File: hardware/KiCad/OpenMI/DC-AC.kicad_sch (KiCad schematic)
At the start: 30 parts, among them Q2 IPL60R125P7, Q3 IPL60R125P7, U1 IRS2304S

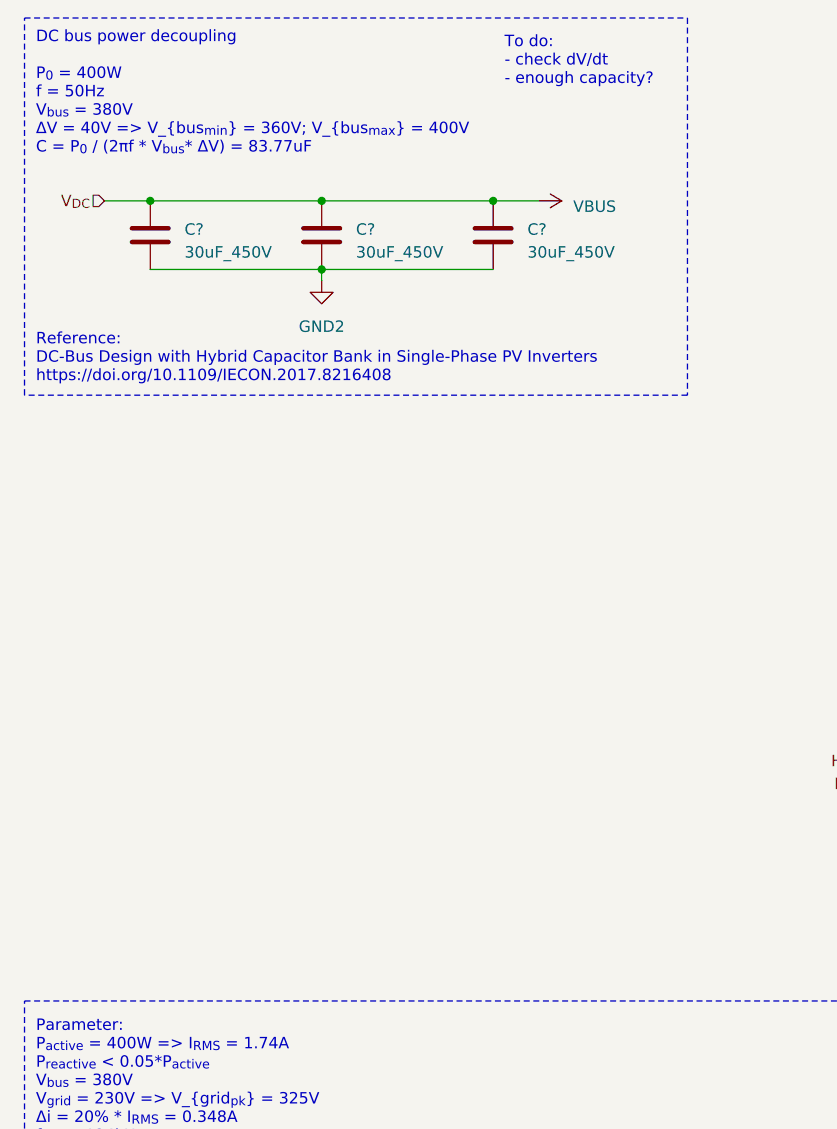
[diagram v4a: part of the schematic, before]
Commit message: feat(hw): Add DC bus voltage sensing
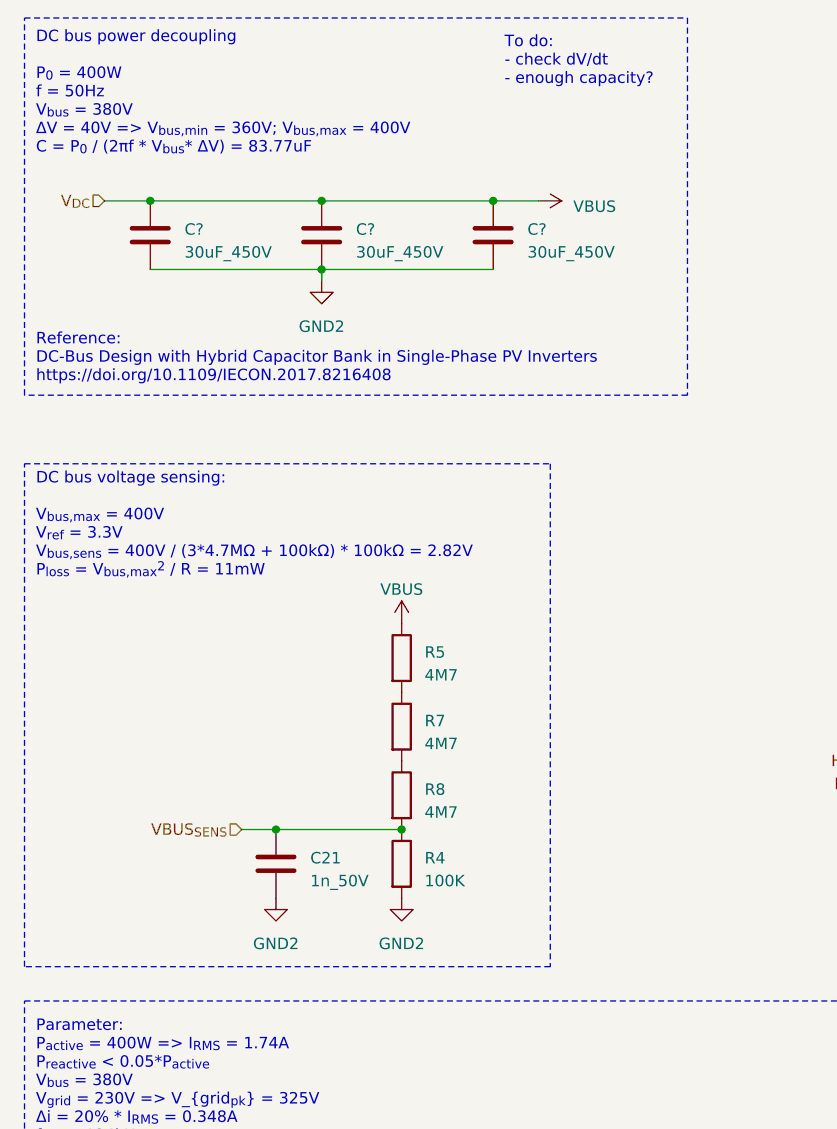
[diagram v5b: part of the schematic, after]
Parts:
- added C21: 1n_50V, Capacitor_SMD:C_0603_1608Metric, symbol _C_0603:1n_50V
- added R4: 100K, Resistor_SMD:R_0603_1608Metric, symbol _R_0603:100K
- added R5, R7, R8: 4M7, Resistor_SMD:R_1206_3216Metric, symbol _R_1206:4M7
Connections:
- net GND: now also C21.2, R4.2
- net VBUS: now also R5.1
- new net: R5.2, R7.1
- new net: R7.2, R8.1
- new net VBUS_{SENS}: C21.1, R4.1, R8.2
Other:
- note added: "DC bus power decoupling P_{0} = 400W f = 50Hz V_{bus} = 380V ΔV = 40V => V_{bus,min} = 360V; V_{bus,max} = 400V C = P_{0} / (2πf * V_{bus}* ΔV) = 83.77uF"
- note added: "DC bus voltage sensing: V_{bus,max} = 400V V_{ref} = 3.3V V_{bus,sens} = 400V / (3*4.7MΩ + 100kΩ) * 100kΩ = 2.82V P_{loss} = V_{bus,max}^{2} / R = 11mW"
- note removed: "DC bus power decoupling P_{0} = 400W f = 50Hz V_{bus} = 380V ΔV = 40V => V_{bus_{min}} = 360V; V_{bus_{max}} = 400V C = P_{0} / (2πf * V_{bus}* ΔV) = 83.77uF"

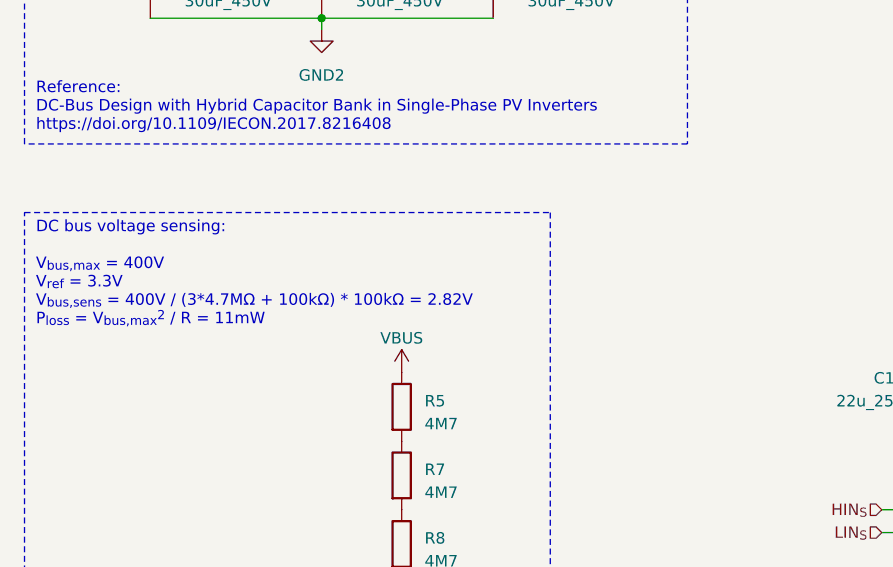
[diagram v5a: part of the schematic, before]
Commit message: docs(hw): adds calculation of voltage divider cutoff frequency
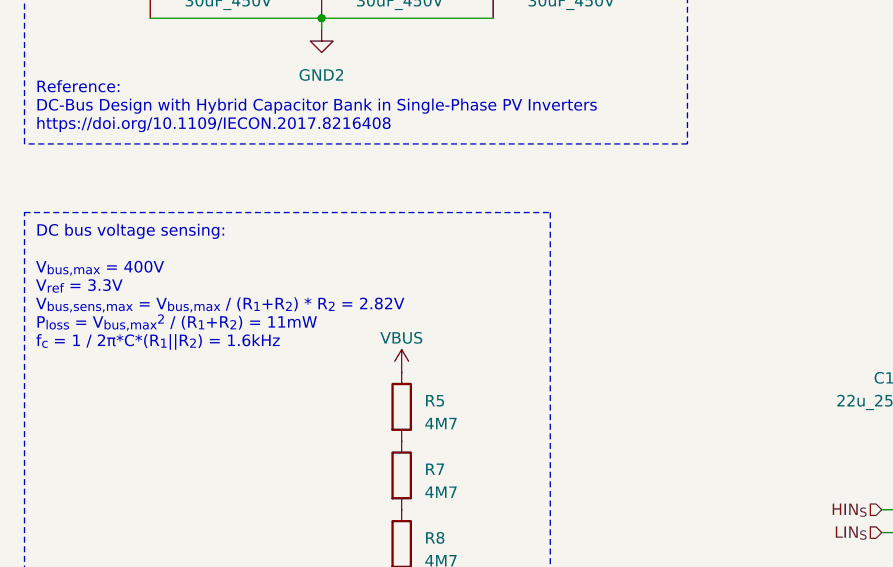
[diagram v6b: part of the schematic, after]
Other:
- note added: "DC bus voltage sensing: V_{bus,max} = 400V V_{ref} = 3.3V V_{bus,sens,max} = V_{bus,max} / (R_{1}+R_{2}) * R_{2} = 2.82V P_{loss} = V_{bus,max}^{2} / (R_{1}+R_{2}) = 11mW f_{c} = 1 / 2π*C*(R_{1}||R_{2}) = 1.6kHz"
- note removed: "DC bus voltage sensing: V_{bus,max} = 400V V_{ref} = 3.3V V_{bus,sens} = 400V / (3*4.7MΩ + 100kΩ) * 100kΩ = 2.82V P_{loss} = V_{bus,max}^{2} / R = 11mW"
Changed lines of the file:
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@@
     (effects (font (size 1.27 1.27)) (justify left bottom) (href "https://intelligentpower.engr.uga.edu/wp-content/uploads/2019/10/deqiang2017Dc-bus.pdf"))
   )
-  (text "DC bus voltage sensing:\n\nV_{bus,max} = 400V\nV_{ref} = 3.3V\nV_{bus,sens} = 400V / (3*4.7MΩ + 100kΩ) * 100kΩ = 2.82V\nP_{loss} = V_{bus,max}^{2} / R = 11mW"
-    (at 17.78 78.74 0)
+  (text "DC bus voltage sensing:\n\nV_{bus,max} = 400V\nV_{ref} = 3.3V\nV_{bus,sens,max} = V_{bus,max} / (R_{1}+R_{2}) * R_{2} = 2.82V\nP_{loss} = V_{bus,max}^{2} / (R_{1}+R_{2}) = 11mW\nf_{c} = 1 / 2π*C*(R_{1}||R_{2}) = 1.6kHz\n"
+    (at 17.78 81.28 0)
     (effects (font (size 1.27 1.27)) (justify left bottom))
   )

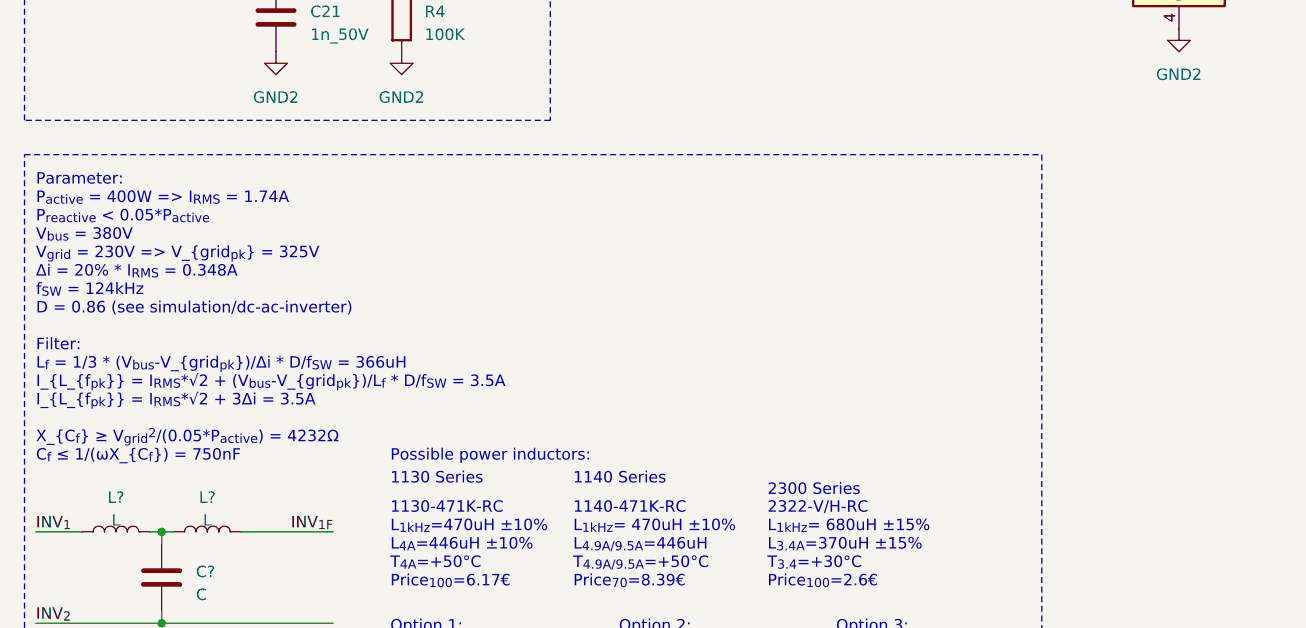
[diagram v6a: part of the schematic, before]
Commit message: docs(hw): Adds parameter and results of Coilcraft Power Inductor Finder
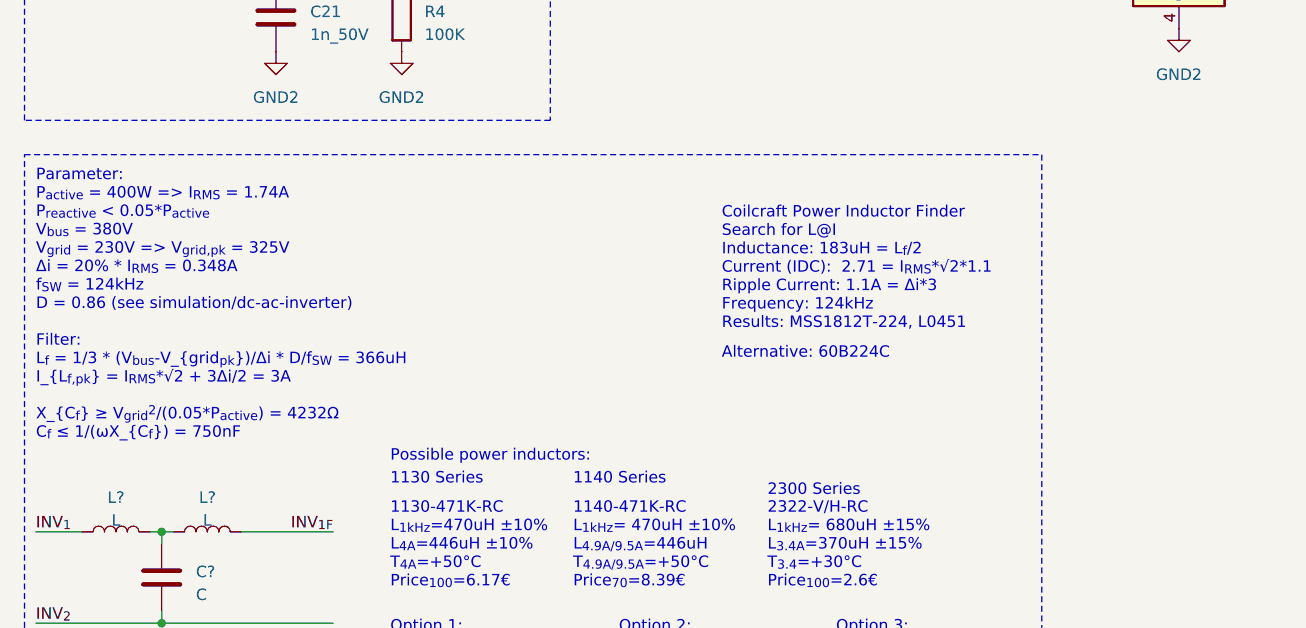
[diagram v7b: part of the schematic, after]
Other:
- note added: "Alternative: 60B224C"
- note added: "Coilcraft Power Inductor Finder Search for L@I Inductance: 183uH = L_{f}/2 Current (IDC): 2.71 = I_{RMS}*√2*1.1 Ripple Current: 1.1A = Δi*3 Frequency: 124kHz Results: MSS1812T-224, L0451"
- note added: "Parameter: P_{active} = 400W => I_{RMS} = 1.74A P_{reactive} < 0.05*P_{active} V_{bus} = 380V V_{grid} = 230V => V_{grid,pk} = 325V Δi = 20% * I_{RMS} = 0.348A f_{SW} = 124kHz D = 0.86 (see simulation/dc-ac-inverter) Filter: L_{f} = 1/3 * (V_{bus}-V_{grid_{pk}})/Δi * D/f_{SW} = 366uH I_{L_{f,pk}} = I_{RMS}*√2 + 3Δi/2 = 3A X_{C_{f}} ≥ V_{grid}^{2}/(0.05*P_{active}) = 4232Ω C_{f} ≤ 1/(ωX_{C_{f}}) =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"
- note removed: "Parameter: P_{active} = 400W => I_{RMS} = 1.74A P_{reactive} < 0.05*P_{active} V_{bus} = 380V V_{grid} = 230V => V_{grid_{pk}} = 325V Δi = 20% * I_{RMS} = 0.348A f_{SW} = 124kHz D = 0.86 (see simulation/dc-ac-inverter) Filter: L_{f} = 1/3 * (V_{bus}-V_{grid_{pk}})/Δi * D/f_{SW} = 366uH I_{L_{f_{pk}}} = I_{RMS}*√2 + (V_{bus}-V_{grid_{pk}})/L_{f} * D/f_{SW} = 3.5A I_{L_{f_{pk}}} = I_{RMS}*√2 + 3Δi 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"
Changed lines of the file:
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@@
     (effects (font (size 1.27 1.27)) (justify left bottom))
   )
-  (text "Parameter:\nP_{active} = 400W => I_{RMS} = 1.74A\nP_{reactive} < 0.05*P_{active}\nV_{bus} = 380V\nV_{grid} = 230V => V_{grid_{pk}} = 325V\nΔi = 20% * I_{RMS} = 0.348A\nf_{SW} = 124kHz\nD = 0.86 (see simulation/dc-ac-inverter)\n\nFilter:\nL_{f} = 1/3 * (V_{bus}-V_{grid_{pk}})/Δi * D/f_{SW} = 366uH\nI_{L_{f_{pk}}} = I_{RMS}*√2 + (V_{bus}-V_{grid_{pk}})/L_{f} * D/f_{SW} = 3.5A\nI_{L_{f_{pk}}} = I_{RMS}*√2 + 3Δi = 3.5A\n\nX_{C_{f}} ≥ V_{grid}^{2}/(0.05*P_{active}) = 4232Ω\nC_{f} ≤ 1/(ωX_{C_{f}}) = 750nF"
-    (at 17.78 160.02 0)
+  (text "Coilcraft Power Inductor Finder\nSearch for L@I\nInductance: 183uH = L_{f}/2\nCurrent (IDC):  2.71 = I_{RMS}*√2*1.1\nRipple Current: 1.1A = Δi*3\nFrequency: 124kHz\nResults: MSS1812T-224, L0451\n\n"
+    (at 93.98 147.32 0)
+    (effects (font (size 1.27 1.27)) (justify left bottom) (href "https://www.coilcraft.com/en-us/tools/power-inductor-finder/"))
+  )
+  (text "Parameter:\nP_{active} = 400W => I_{RMS} = 1.74A\nP_{reactive} < 0.05*P_{active}\nV_{bus} = 380V\nV_{grid} = 230V => V_{grid,pk} = 325V\nΔi = 20% * I_{RMS} = 0.348A\nf_{SW} = 124kHz\nD = 0.86 (see simulation/dc-ac-inverter)\n\nFilter:\nL_{f} = 1/3 * (V_{bus}-V_{grid_{pk}})/Δi * D/f_{SW} = 366uH\nI_{L_{f,pk}} = I_{RMS}*√2 + 3Δi/2 = 3A\n\nX_{C_{f}} ≥ V_{grid}^{2}/(0.05*P_{active}) = 4232Ω\nC_{f} ≤ 1/(ωX_{C_{f}}) = 750nF"
+    (at 17.78 157.48 0)
     (effects (font (size 1.27 1.27)) (justify left bottom))
   )
+  (text "Alternative: 60B224C" (at 93.98 148.59 0)
+    (effects (font (size 1.27 1.27)) (justify left bottom) (href "https://search.murata.co.jp/Ceramy/image/img/P02A/kmp_6000b.pdf"))
+  )
   (text "1140 Series" (at 77.47 162.56 0)

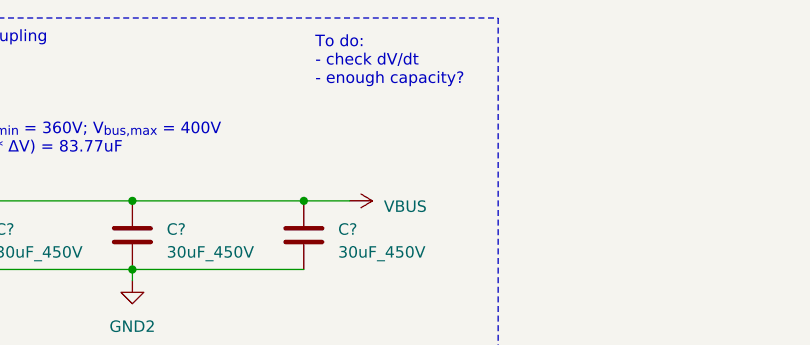
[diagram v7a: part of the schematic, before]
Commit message: docs(hw): update DC Bus power decoupling to dos
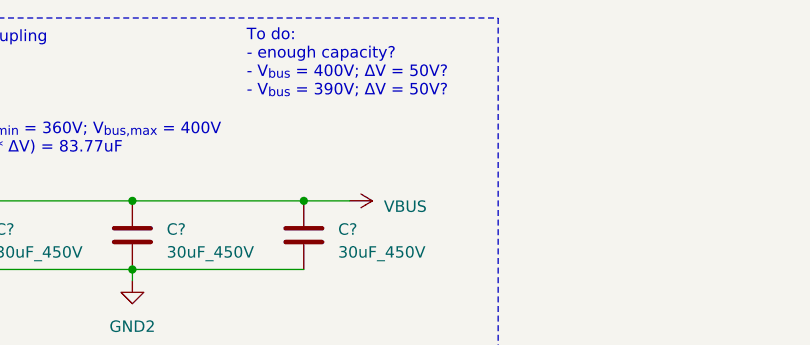
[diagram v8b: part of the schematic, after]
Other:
- note added: "To do: - enough capacity? - V_{bus} = 400V; ΔV = 50V? - V_{bus} = 390V; ΔV = 50V?"
- note removed: "To do: - check dV/dt - enough capacity?"
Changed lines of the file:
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@@
     (effects (font (size 1.27 1.27)) (justify left bottom))
   )
-  (text "To do:\n- check dV/dt\n- enough capacity?" (at 69.85 24.13 0)
+  (text "To do:\n- enough capacity?\n- V_{bus} = 400V; ΔV = 50V?\n- V_{bus} = 390V; ΔV = 50V?"
+    (at 62.23 25.4 0)
     (effects (font (size 1.27 1.27)) (justify left bottom))
   )
